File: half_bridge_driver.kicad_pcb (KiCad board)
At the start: 2 copper layers, 23 x 6 mm, 7 parts, among them J2 Conn_01x01_Male, U1 ZXGD3003E6, U2 ZXGD3003E6

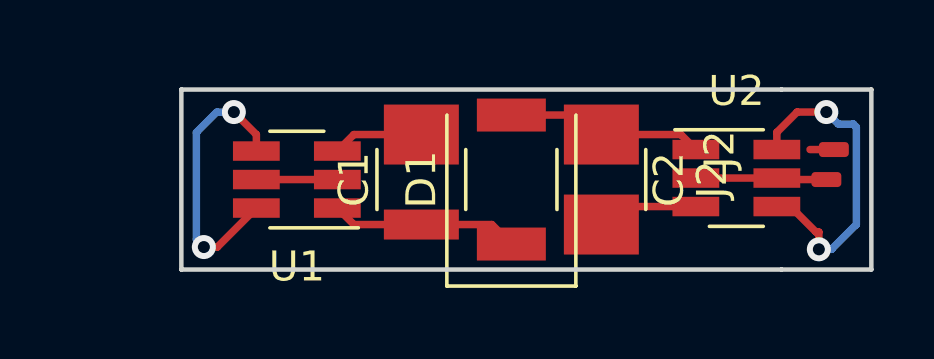
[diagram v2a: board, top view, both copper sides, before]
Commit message: Added extra pad for input and output driver signals to ease wire soldering.
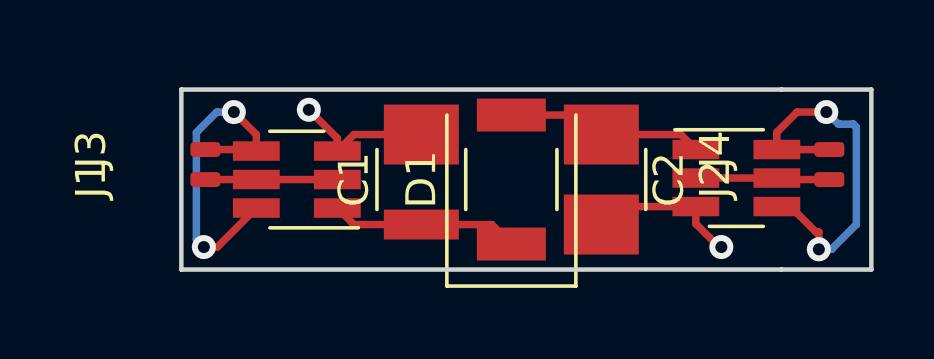
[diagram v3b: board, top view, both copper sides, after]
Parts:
- removed the J2 at (157.2, 89.0)
- added J1: Conn_01x01_Male, Wire_Pads:SolderWirePad_single_SMD_5x10mm, F.Cu at (136.3, 90.0)
- added J3: Conn_01x01_Male, Wire_Pads:SolderWirePad_single_SMD_5x10mm, F.Cu at (136.3, 89.0)
- added J4: Conn_01x01_Male, Wire_Pads:SolderWirePad_single_SMD_5x10mm, F.Cu at (157.1, 89.0)
- moved J2 0.10 mm to (157.1, 90.0)
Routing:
- net /GND_High_Side: track 3.03 -> 4.80 mm, vias 0 -> 1
- net /Low_Side_MOSFET_Gate: track 10.9 -> 12.6 mm
- net GND: track 3.40 -> 5.14 mm, vias 0 -> 1
- net /High_Side_MOSFET_Gate: track 9.35 -> 11.1 mm
- net /High_Side_Input: track 2.70 -> 4.40 mm
- net (no net): track 0.54 -> 0.00 mm
- added copper zone on B.Cu, net /GND_High_Side
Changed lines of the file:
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@@
     (thickness 1.6)
     (drawings 6)
-    (tracks 42)
+    (tracks 52)
     (zones 0)
-    (modules 7)
+    (modules 9)
     (nets 9)
   )
@@
     (45 Margin user)
     (46 B.CrtYd user)
-    (47 F.CrtYd user)
+    (47 F.CrtYd user hide)
     (48 B.Fab user)
     (49 F.Fab user)
@@
       (outputformat 1)
       (mirror false)
-      (drillshape 1)
+      (drillshape 0)
       (scaleselection 1)
-      (outputdirectory ""))
+      (outputdirectory "Gerber/"))
   )
   (net 0 "")
@@
   )
   (module Wire_Pads:SolderWirePad_single_SMD_5x10mm (layer F.Cu)
-    (at 157.25 89 90)
+    (at 157.1 89 90)
     (descr "Wire Pad, Square, SMD Pad,  5mm x 10mm,")
     (tags "MesurementPoint Square SMDPad 5mmx10mm ")
     (attr smd)
-    (fp_text reference J2 (at 0 -3.81 90) (layer F.SilkS)
+    (fp_text reference J4 (at 0 -3.81 90) (layer F.SilkS)
       (effects (font (size 1 1) (thickness 0.15)))
     )
@@
     (fp_line (start 2.75 -5.25) (end -2.75 -5.25) (layer F.CrtYd) (width 0.05))
     (pad 1 smd roundrect (at 0 0 90) (size 0.5 1) (layers F.Cu F.Paste F.Mask) (roundrect_rratio 0.25)
-      (zone_connect 0))
+      (net 8 /Low_Side_MOSFET_Gate))
+  )
+  (module Wire_Pads:SolderWirePad_single_SMD_5x10mm (layer F.Cu)
+    (at 136.3 89 90)
+    (descr "Wire Pad, Square, SMD Pad,  5mm x 10mm,")
+    (tags "MesurementPoint Square SMDPad 5mmx10mm ")
+    (attr smd)
+    (fp_text reference J3 (at 0 -3.81 90) (layer F.SilkS)
+      (effects (font (size 1 1) (thickness 0.15)))
+    )
+    (fp_text value Conn_01x01_Male (at 0 6.35 90) (layer F.Fab) hide
+      (effects (font (size 1 1) (thickness 0.15)))
+    )
+    (fp_line (start 2.75 -5.25) (end -2.75 -5.25) (layer F.CrtYd) (width 0.05))
+    (fp_line (start 2.75 5.25) (end 2.75 -5.25) (layer F.CrtYd) (width 0.05))
+    (fp_line (start -2.75 5.25) (end 2.75 5.25) (layer F.CrtYd) (width 0.05))
+    (fp_line (start -2.75 -5.25) (end -2.75 5.25) (layer F.CrtYd) (width 0.05))
+    (pad 1 smd roundrect (at 0 0 90) (size 0.5 1) (layers F.Cu F.Paste F.Mask) (roundrect_rratio 0.25)
+      (net 7 /High_Side_MOSFET_Gate))
+  )
+  (module Wire_Pads:SolderWirePad_single_SMD_5x10mm (layer F.Cu)
+    (at 136.3 90 90)
+    (descr "Wire Pad, Square, SMD Pad,  5mm x 10mm,")
+    (tags "MesurementPoint Square SMDPad 5mmx10mm ")
+    (attr smd)
+    (fp_text reference J1 (at 0 -3.81 90) (layer F.SilkS)
+      (effects (font (size 1 1) (thickness 0.15)))
+    )
+    (fp_text value Conn_01x01_Male (at 0 6.35 90) (layer F.Fab) hide
+      (effects (font (size 1 1) (thickness 0.15)))
+    )
+    (fp_line (start -2.75 -5.25) (end -2.75 5.25) (layer F.CrtYd) (width 0.05))
+    (fp_line (start -2.75 5.25) (end 2.75 5.25) (layer F.CrtYd) (width 0.05))
+    (fp_line (start 2.75 5.25) (end 2.75 -5.25) (layer F.CrtYd) (width 0.05))
+    (fp_line (start 2.75 -5.25) (end -2.75 -5.25) (layer F.CrtYd) (width 0.05))
+    (pad 1 smd roundrect (at 0 0 90) (size 0.5 1) (layers F.Cu F.Paste F.Mask) (roundrect_rratio 0.25)
+      (net 5 /High_Side_Input))
   )
   (module Capacitors_SMD:C_1210 (layer F.Cu)
@@
       (effects (font (size 1 1) (thickness 0.15)))
     )
-    (fp_text value GB01SLT12-214 (at 0 3.1 90) (layer F.Fab)
+    (fp_text value GB01SLT12-214 (at 0 3.1 90) (layer F.Fab) hide
       (effects (font (size 1 1) (thickness 0.15)))
     )
@@
   )
   (module Wire_Pads:SolderWirePad_single_SMD_5x10mm (layer F.Cu)
-    (at 157 90 90)
+    (at 157.1 90 90)
     (descr "Wire Pad, Square, SMD Pad,  5mm x 10mm,")
     (tags "MesurementPoint Square SMDPad 5mmx10mm ")
@@
     (tags "SOT-23-6 Handsoldering")
     (attr smd)
-    (fp_text reference U1 (at 0 -2.9 180) (layer F.SilkS)
+    (fp_text reference U1 (at 0 -2.9 180) (layer F.SilkS) hide
       (effects (font (size 1 1) (thickness 0.15)))
     )
@@
     (tags "SOT-23-6 Handsoldering")
     (attr smd)
-    (fp_text reference U2 (at 0 -2.9) (layer F.SilkS)
+    (fp_text reference U2 (at 0 -2.9) (layer F.SilkS) hide
       (effects (font (size 1 1) (thickness 0.15)))
     )
@@
   (gr_line (start 155.5 93) (end 135.5 93) (layer Edge.Cuts) (width 0.15))
   (gr_line (start 135.5 87) (end 155.5 87) (layer Edge.Cuts) (width 0.15))
-  (segment (start 157 89) (end 156.455001 89) (width 0.25) (layer F.Cu) (net 0))
   (segment (start 141.25 88.5) (end 140.7 89.05) (width 0.25) (layer F.Cu) (net 1))
   (segment (start 143.5 88.5) (end 141.25 88.5) (width 0.25) (layer F.Cu) (net 1))
+  (via (at 139.75 87.675) (size 0.8) (drill 0.4) (layers F.Cu B.Cu) (net 1))
+  (segment (start 140.7 89.05) (end 140.7 88.625) (width 0.25) (layer F.Cu) (net 1))
+  (segment (start 140.7 88.625) (end 139.75 87.675) (width 0.25) (layer F.Cu) (net 1))
   (segment (start 145.85 91.5) (end 146.5 92.15) (width 0.25) (layer F.Cu) (net 2))
   (segment (start 143.5 91.5) (end 145.85 91.5) (width 0.25) (layer F.Cu) (net 2))
@@
   (segment (start 150.1 90.9) (end 149.5 91.5) (width 0.25) (layer F.Cu) (net 4))
   (segment (start 152.65 90.9) (end 150.1 90.9) (width 0.25) (layer F.Cu) (net 4))
+  (segment (start 152.65 91.475) (end 153.425 92.25) (width 0.25) (layer F.Cu) (net 4))
+  (segment (start 152.65 90.9) (end 152.65 91.475) (width 0.25) (layer F.Cu) (net 4))
+  (via (at 153.5 92.25) (size 0.8) (drill 0.4) (layers F.Cu B.Cu) (net 4))
+  (segment (start 153.425 92.25) (end 153.5 92.25) (width 0.25) (layer F.Cu) (net 4))
   (segment (start 140.7 90) (end 138 90) (width 0.25) (layer F.Cu) (net 5))
+  (segment (start 136.3 90) (end 138 90) (width 0.25) (layer F.Cu) (net 5))
   (segment (start 155.35 89.95) (end 152.65 89.95) (width 0.25) (layer F.Cu) (net 6))
   (segment (start 155.4 90) (end 155.35 89.95) (width 0.25) (layer F.Cu) (net 6))
@@
   (segment (start 136.7 92.25) (end 138 90.95) (width 0.25) (layer F.Cu) (net 7))
   (segment (start 136.25 92.25) (end 136.7 92.25) (width 0.25) (layer F.Cu) (net 7))
+  (segment (start 137.95 89) (end 138 89.05) (width 0.25) (layer F.Cu) (net 7))
+  (segment (start 136.3 89) (end 137.95 89) (width 0.25) (layer F.Cu) (net 7))
   (segment (start 155.35 88.425) (end 156.025 87.75) (width 0.25) (layer F.Cu) (net 8))
   (segment (start 155.35 89) (end 155.35 88.425) (width 0.25) (layer F.Cu) (net 8))
@@
   (segment (start 156.655 91.75) (end 155.805 90.9) (width 0.25) (layer F.Cu) (net 8))
   (segment (start 156.75 91.75) (end 156.655 91.75) (width 0.25) (layer F.Cu) (net 8))
+  (segment (start 157.1 89) (end 155.35 89) (width 0.25) (layer F.Cu) (net 8))
   (zone (net 4) (net_name GND) (layer F.Cu) (hatch edge 0.508)
     (connect_pads (clearance 0.508))
@@
       )
     )
+  )
+  (zone (net 1) (net_name /GND_High_Side) (layer B.Cu) (hatch edge 0.508)
+    (connect_pads (clearance 0.508))
+    (min_thickness 0.254)
+    (fill yes (arc_segments 16) (thermal_gap 0.508) (thermal_bridge_width 0.508))
+    (polygon
+      (pts
+        (xy 135.5 87) (xy 135.5 93) (xy 158.5 93) (xy 158.5 87)
+      )
+    )
